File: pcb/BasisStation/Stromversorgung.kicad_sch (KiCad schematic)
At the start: 13 parts

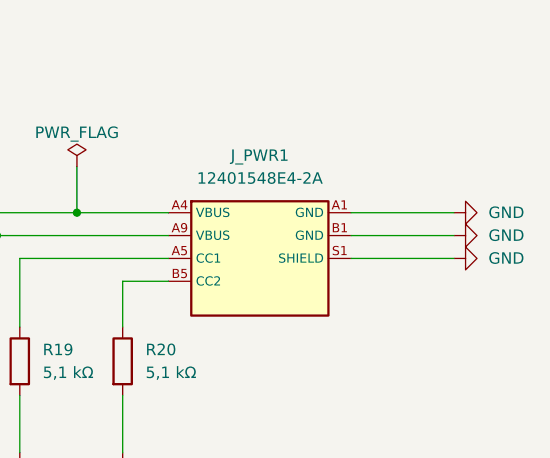
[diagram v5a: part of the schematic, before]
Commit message: v0.00.001 feat(SHBS-6): Debug-Anschluss J1 von USB-B-Micro auf USB-C umgestellt
J1 durch Connector:USB_C_Receptacle_USB2.0_16P ersetzt, bestueckt mit der
Amphenol 12401548E4-2A - derselben Buchse wie der Versorgungsport J_PWR1,
also ohne zusaetzliche BOM-Position.

Beide Datenpaare (A6/B6 und A7/B7) gebrueckt, damit der Stecker in beiden
Orientierungen funktioniert. CC1/CC2 mit je 5,1 kOhm Rd gegen GND (R21, R22)
fuer Sink-Betrieb. Footprint zugewiesen, Netz 5VUSB in VBUS_J1 umbenannt.
VBUS bleibt unbeschaltet - Versorgung laeuft weiterhin ausschliesslich ueber
J_PWR1.

Der GND-Pin des alten USB_B_Micro-Symbols war als Power output deklariert
und damit unbemerkt der einzige ERC-Treiber des globalen GND-Netzes.
Ersetzt durch PWR_FLAG #FLG04 am GND-Draht von J_PWR1.A1.

ERC: 0 Fehler, 9 Warnungen (saemtlich Altbestand).

Co-Authored-By: Claude Opus 5 <noreply@anthropic.com>
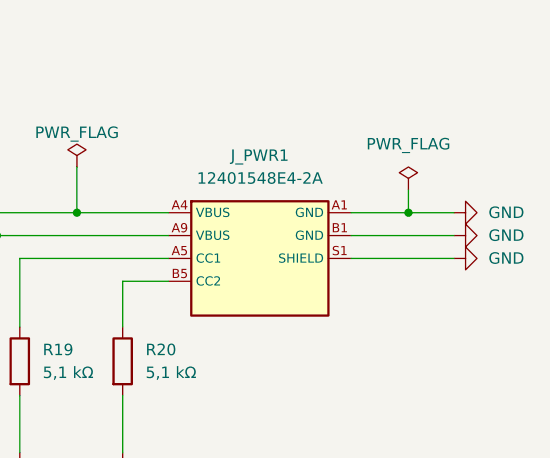
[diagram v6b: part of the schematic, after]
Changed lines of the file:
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@@
+	)
+	(junction
+		(at 262.89 78.74)
+		(diameter 0)
+		(color 0 0 0 0)
 	)
 	(junction
@@
 	(wire
 		(pts
-			(xy 256.54 78.74) (xy 267.97 78.74)
+			(xy 256.54 78.74) (xy 262.89 78.74)
 		)
 		(stroke
@@
 	(wire
 		(pts
+			(xy 262.89 76.2) (xy 262.89 78.74)
+		)
+		(stroke
+			(width 0)
+			(type default)
+		)
+	)
+	(wire
+		(pts
 			(xy 185.42 138.43) (xy 190.5 138.43)
 		)
@@
 		(pts
 			(xy 167.64 76.2) (xy 167.64 83.82)
+		)
+		(stroke
+			(width 0)
+			(type default)
+		)
+	)
+	(wire
+		(pts
+			(xy 262.89 78.74) (xy 267.97 78.74)
 		)
 		(stroke
@@
 					(unit 1)
 				)
+			)
+		)
+	)
+	(symbol
+		(lib_id "power:PWR_FLAG")
+		(at 262.89 76.2 0)
+		(unit 1)
+		(exclude_from_sim no)
+		(in_bom yes)
+		(on_board yes)
+		(dnp no)
+		(fields_autoplaced yes)
+		(property "Reference" "#FLG04"
+			(at 262.89 74.295 0)
+			(effects
+				(font
+					(size 1.27 1.27)
+				)
+				(hide yes)
+			)
+		)
+		(property "Value" "PWR_FLAG"
+			(at 262.89 71.12 0)
+			(effects
+				(font
+					(size 1.27 1.27)
+				)
+			)
+		)
+		(property "Footprint" ""
+			(at 262.89 76.2 0)
+			(effects
+				(font
+					(size 1.27 1.27)
+				)
+				(hide yes)
+			)
+		)
+		(property "Datasheet" "~"
+			(at 262.89 76.2 0)
+			(effects
+				(font
+					(size 1.27 1.27)
+				)
+				(hide yes)
+			)
+		)
+		(property "Description" "Special symbol for telling ERC where power comes from"
+			(at 262.89 76.2 0)
+			(effects
+				(font
+					(size 1.27 1.27)
+				)
+				(hide yes)
+			)
+		)
+		(pin "1"
+		)
+		(instances
+			(project ""
+				(path "/498c7092-55c1-4229-9f4b-13c6a8e7da47/5fd3b213-b7bb-4f0b-b520-d744bf60efa7"
+					(reference "#FLG04")
+					(unit 1)
+				)

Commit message: v0.00.001 refactor(SHBS-12): KiCad-Bibliotheken auf Bauteilordner umgestellt
Symbol, Footprint und 3D-Modell eines Bauteils lagen bisher in drei
getrennten Sammelordnern. Jedes Bauteil hat jetzt einen eigenen Ordner
unter pcb/Bauteile/; pcb/Symbol/, pcb/Footprints/ und pcb/3D-Model/
entfallen.

Umfang: 20 Dateien verschoben, 13 verwaiste entfernt, 63 Footprint-
Referenzen in Schaltplaenen, Netzliste und Board umgeschrieben, 7
Footprint-Vorgaben in den Symbol-Dateien angepasst.

Nebenbei behoben:
- Die 3D-Modelle waren im Board ueber absolute Pfade auf E: und in der
  Netzliste auf C: verdrahtet, funktionsfaehig jeweils nur auf einem
  Rechner. Jetzt durchgaengig ueber ${KIPRJMOD}.
- Drei Footprint-Referenzen zeigten auf Bibliotheken, die nie in der
  fp-lib-table standen.
- WCAP-FTXX_P10 hatte keine Footprint-Vorgabe, der W5500-Footprint keine
  3D-Referenz.
- fp-info-cache und *.kicad_prl sind nicht mehr versioniert.

Verifikation: Projekt oeffnet ohne Bibliotheks-Warnung. ERC 0 Fehler und
7 Warnungen, vorher 9, keine neue. DRC meldet "Found 0 Footprint errors";
der verbliebene DRC-Fehler ist eine vorbestehende Routing-Luecke im
EN-Netz. 3D-Ansicht zeigt die Modelle.

Co-Authored-By: Claude Opus 5 <noreply@anthropic.com>
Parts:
- J_PWR1: footprint Footprints:USB_C_Receptacle_Amphenol_12401548E4-2A -> shbs_power:USB_C_Receptacle_Amphenol_12401548E4-2A
- PS1: footprint Footprints:MP2359DJ -> shbs_power:MP2359DJ
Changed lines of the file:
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@@
 			)
 		)
-		(property "Footprint" "Footprints:USB_C_Receptacle_Amphenol_12401548E4-2A"
+		(property "Footprint" "shbs_power:USB_C_Receptacle_Amphenol_12401548E4-2A"
 			(at 246.38 83.82 0)
 			(effects
@@
 			)
 		)
-		(property "Footprint" "Footprints:MP2359DJ"
+		(property "Footprint" "shbs_power:MP2359DJ"
 			(at 148.59 86.36 0)
 			(effects
